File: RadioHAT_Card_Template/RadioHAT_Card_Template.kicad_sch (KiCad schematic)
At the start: 1 part

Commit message: Fix errors in template
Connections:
- net NSS1: now reaches J1.20 (NSS1)
- net NSS0: now reaches J1.51 (NSS0)
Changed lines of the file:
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@@
 	(wire
 		(pts
-			(xy 26.67 44.45) (xy 33.02 44.45)
+			(xy 26.67 46.99) (xy 33.02 46.99)
 		)
 		(stroke
@@
 	(wire
 		(pts
+			(xy 26.67 57.15) (xy 33.02 57.15)
+		)
+		(stroke
+			(width 0)
+			(type default)
+		)
+	)
+	(wire
+		(pts
 			(xy 52.07 25.4) (xy 52.07 27.94)
 		)
@@
 		)
 	)
-	(global_label "NSS"
-		(shape input)
-		(at 26.67 44.45 180)
-		(fields_autoplaced yes)
-		(effects
-			(font
-				(size 1.27 1.27)
-			)
-			(justify right)
-		)
-		(property "Intersheetrefs" "${INTERSHEET_REFS}"
-			(at 19.9353 44.45 0)
+	(global_label "NSS0"
+		(shape input)
+		(at 26.67 46.99 180)
+		(fields_autoplaced yes)
+		(effects
+			(font
+				(size 1.27 1.27)
+			)
+			(justify right)
+		)
+		(property "Intersheetrefs" "${INTERSHEET_REFS}"
+			(at 18.7258 46.99 0)
 			(effects
 				(font
@@
 			(effects
 				(font
+					(size 1.27 1.27)
+				)
+				(justify right)
+				(hide yes)
+			)
+		)
+	)
+	(global_label "NSS1"
+		(shape input)
+		(at 26.67 57.15 180)
+		(fields_autoplaced yes)
+		(effects
+			(font
+				(size 1.27 1.27)
+			)
+			(justify right)
+		)
+		(property "Intersheetrefs" "${INTERSHEET_REFS}"
+			(at 18.7258 57.15 0)
+			(effects
+				(font

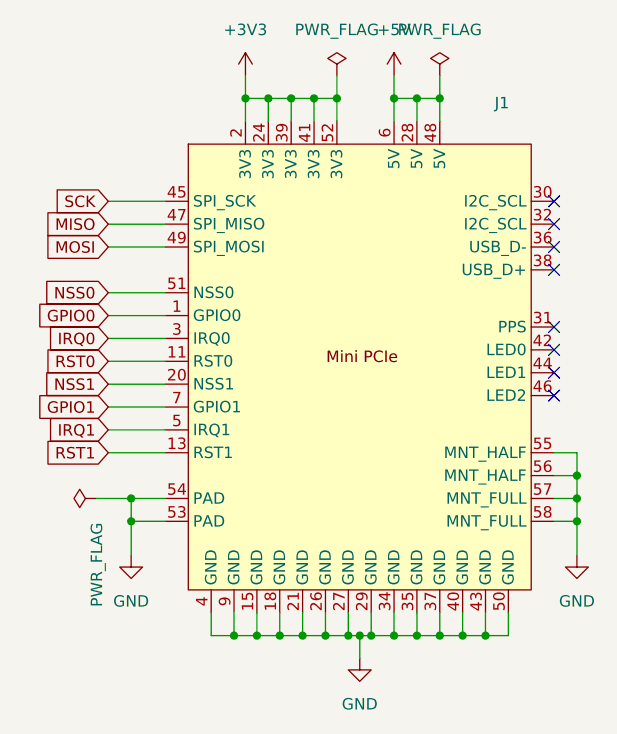
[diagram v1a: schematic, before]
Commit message: Try to fix library symbol mismatch
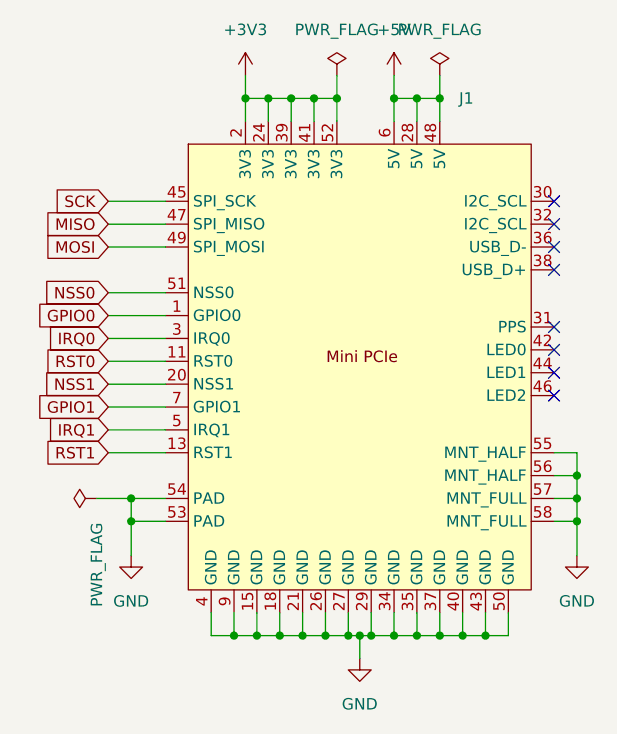
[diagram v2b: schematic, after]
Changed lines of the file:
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@@
+	)
+	(symbol
+		(lib_id "RadioHAT:Mini_PCIe")
+		(at 54.61 54.61 0)
+		(unit 1)
+		(exclude_from_sim no)
+		(in_bom yes)
+		(on_board yes)
+		(dnp no)
+		(fields_autoplaced yes)
+		(property "Reference" "J1"
+			(at 65.6433 25.4 0)
+			(effects
+				(font
+					(size 1.27 1.27)
+				)
+				(justify left)
+			)
+		)
+		(property "Value" "~"
+			(at 65.6433 27.94 0)
+			(effects
+				(font
+					(size 1.27 1.27)
+				)
+				(justify left)
+			)
+		)
+		(property "Footprint" "RadioHAT:Mini_PCIe_Full"
+			(at 59.69 67.31 0)
+			(effects
+				(font
+					(size 1.27 1.27)
+				)
+				(hide yes)
+			)
+		)
+		(property "Datasheet" ""
+			(at 59.69 67.31 0)
+			(effects
+				(font
+					(size 1.27 1.27)
+				)
+				(hide yes)
+			)
+		)
+		(property "Description" ""
+			(at 59.69 67.31 0)
+			(effects
+				(font
+					(size 1.27 1.27)
+				)
+				(hide yes)
+			)
+		)
+		(property "Mouser" "571-1775838-2"
+			(at 54.864 56.388 0)
+			(effects
+				(font
+					(size 1.27 1.27)
+				)
+				(hide yes)
+			)
+		)
+		(pin "3"
+		)
+		(pin "48"
+		)
+		(pin "34"
+		)
+		(pin "47"
+		)
+		(pin "31"
+		)
+		(pin "1"
+		)
+		(pin "9"
+		)
+		(pin "54"
+		)
+		(pin "24"
+		)
+		(pin "57"
+		)
+		(pin "4"
+		)
+		(pin "18"
+		)
+		(pin "29"
+		)
+		(pin "50"
+		)
+		(pin "55"
+		)
+		(pin "28"
+		)
+		(pin "35"
+		)
+		(pin "51"
+		)
+		(pin "15"
+		)
+		(pin "40"
+		)
+		(pin "21"
+		)
+		(pin "43"
+		)
+		(pin "37"
+		)
+		(pin "7"
+		)
+		(pin "5"
+		)
+		(pin "36"
+		)
+		(pin "2"
+		)
+		(pin "41"
+		)
+		(pin "52"
+		)
+		(pin "42"
+		)
+		(pin "46"
+		)
+		(pin "32"
+		)
+		(pin "13"
+		)
+		(pin "27"
+		)
+		(pin "30"
+		)
+		(pin "44"
+		)
+		(pin "49"
+		)
+		(pin "53"
+		)
+		(pin "39"
+		)
+		(pin "26"
+		)
+		(pin "6"
+		)
+		(pin "45"
+		)
+		(pin "38"
+		)
+		(pin "56"
+		)
+		(pin "20"
+		)
+		(pin "11"
+		)
+		(pin "58"
+		)
+		(instances
+			(project ""
+				(path "/61a69050-cb5e-4dbc-87a1-bbbff559bb0e"
+					(reference "J1")
+					(unit 1)
+				)
+			)
+		)
 	)
 	(symbol
@@
 					(unit 1)
 				)
-			)
-		)
-	)
-	(symbol
-		(lib_id "RadioHAT:Mini_PCIe")
-		(at 54.61 54.61 0)
-		(unit 1)
-		(exclude_from_sim no)
-		(in_bom yes)
-		(on_board yes)
-		(dnp no)
-		(property "Reference" "J1"
-			(at 69.596 25.908 0)
-			(effects
-				(font
-					(size 1.27 1.27)
-				)
-				(justify left)
-			)
-		)
-		(property "Value" "~"
-			(at 61.8333 27.94 0)
-			(effects
-				(font
-					(size 1.27 1.27)
-				)
-				(justify left)
-			)
-		)
-		(property "Footprint" "RadioHAT:Mini_PCIe_Full"
-			(at 59.69 67.31 0)
-			(effects
-				(font
-					(size 1.27 1.27)
-				)
-				(hide yes)
-			)
-		)
-		(property "Datasheet" ""
-			(at 59.69 67.31 0)
-			(effects
-				(font
-					(size 1.27 1.27)
-				)
-				(hide yes)
-			)
-		)
-		(property "Description" ""
-			(at 59.69 67.31 0)
-			(effects
-				(font
-					(size 1.27 1.27)
-				)
-				(hide yes)
-			)
-		)
-		(property "Mouser" "571-1775838-2"
-			(at 54.61 54.61 0)
-			(effects
-				(font
-					(size 1.27 1.27)
-				)
-				(hide yes)
-			)
-		)
-		(pin "51"
-		)
-		(pin "13"
-		)
-		(pin "39"
-		)
-		(pin "41"
-		)
-		(pin "52"
-		)
-		(pin "3"
-		)
-		(pin "5"
-		)
-		(pin "9"
-		)
-		(pin "2"
-		)
-		(pin "26"
-		)
-		(pin "49"
-		)
-		(pin "1"
-		)
-		(pin "11"
-		)
-		(pin "7"
-		)
-		(pin "54"
-		)
-		(pin "53"
-		)
-		(pin "4"
-		)
-		(pin "18"
-		)
-		(pin "15"
-		)
-		(pin "24"
-		)
-		(pin "21"
-		)
-		(pin "27"
-		)
-		(pin "29"
-		)
-		(pin "34"
-		)
-		(pin "35"
-		)
-		(pin "37"
-		)
-		(pin "40"
-		)
-		(pin "43"
-		)
-		(pin "50"
-		)
-		(pin "46"
-		)
-		(pin "42"
-		)
-		(pin "56"
-		)
-		(pin "36"
-		)
-		(pin "57"
-		)
-		(pin "44"
-		)
-		(pin "30"
-		)
-		(pin "55"
-		)
-		(pin "31"
-		)
-		(pin "32"
-		)
-		(pin "58"
-		)
-		(pin "38"
-		)
-		(pin "47"
-		)
-		(pin "45"
-		)
-		(pin "20"
-		)
-		(pin "6"
-		)
-		(pin "28"
-		)
-		(pin "48"
-		)
-		(instances
-			(project "RadioHAT_Card_Template"
-				(path "/61a69050-cb5e-4dbc-87a1-bbbff559bb0e"
-					(reference "J1")
-					(unit 1)
-				)
